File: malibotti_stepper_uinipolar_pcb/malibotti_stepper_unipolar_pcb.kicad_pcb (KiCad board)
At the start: 2 copper layers, 70 x 68 mm, 35 parts, among them J1 Stepper 1, J2 Stepper 2, J3 Servo, J4 I2C, J5 USB_C_Receptacle_USB2.0_16P, J6 Serial, SW1 RST, SW2 MicroSwitchLeft, SW3 MicroSwitchRight, SW8 BTN, U1 TBD62783A, U3 AMS1117, U5 ESP32-S3-MINI-1

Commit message: Varions
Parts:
- moved ST1 8.14 mm to (60.5, 76.0)
- moved ST2 8.14 mm to (60.5, 124.0)
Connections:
- J1 pad 1: Net-(J1-Pin_1) -> GND
- J1 pad 5: +5V -> Net-(J1-Pin_5)
- J2 pad 1: Net-(J2-Pin_1) -> GND
- J2 pad 5: +5V -> Net-(J2-Pin_5)
- U1 pad 11: Net-(J1-Pin_1) -> Net-(J1-Pin_5)
- U1 pad 12: Net-(J2-Pin_4) -> Net-(J2-Pin_2)
- U1 pad 13: Net-(J1-Pin_2) -> Net-(J1-Pin_4)
- U1 pad 16: Net-(J2-Pin_2) -> Net-(J2-Pin_4)
- U1 pad 17: Net-(J1-Pin_4) -> Net-(J1-Pin_2)
- U1 pad 18: Net-(J2-Pin_1) -> Net-(J2-Pin_5)
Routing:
- net +5V: track 139.3 -> 117.4 mm
- net Net-(J2-Pin_1): track 14.3 -> 0.00 mm
- net Net-(J2-Pin_2): track 12.3 -> 0.00 mm
- net Net-(J2-Pin_3): track 11.6 -> 0.00 mm
- net Net-(J2-Pin_4): track 10.7 -> 0.00 mm
- net Net-(J1-Pin_1): track 7.75 -> 0.00 mm
- net Net-(J1-Pin_2): track 7.25 -> 0.00 mm
- net Net-(J1-Pin_4): track 7.04 -> 0.00 mm
- net Net-(J1-Pin_3): track 6.75 -> 0.00 mm
- net Net-(J1-Pin_5): track 0.00 -> 3.06 mm
- net GND: vias 136 -> 119

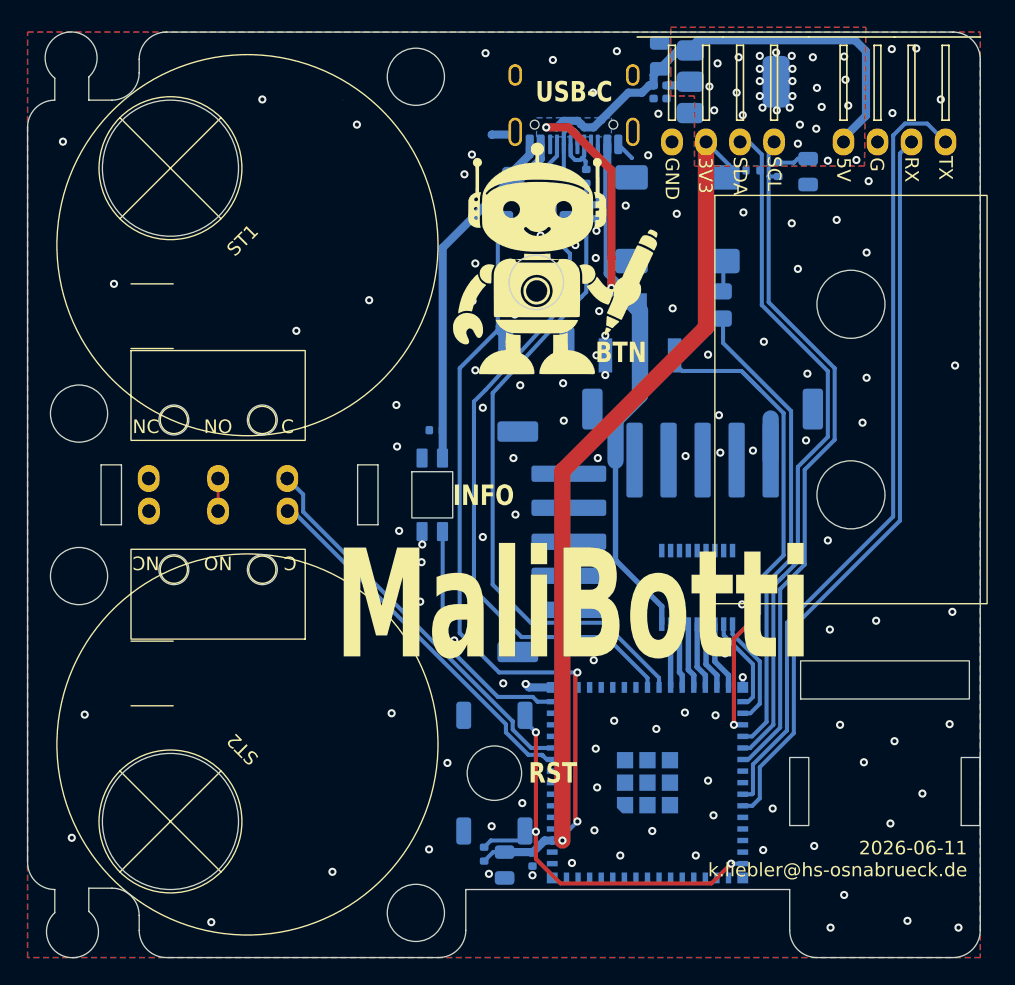
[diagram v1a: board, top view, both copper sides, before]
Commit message: Revert "Merge branch 'master' of https://github.com/klaus-liebler/malibotti"
This reverts commit e32d648555214dd673c0994955a1c8da412dea1e, reversing
changes made to 1ab6b0115ca777e0c305d243220f439b6c76d3ff.
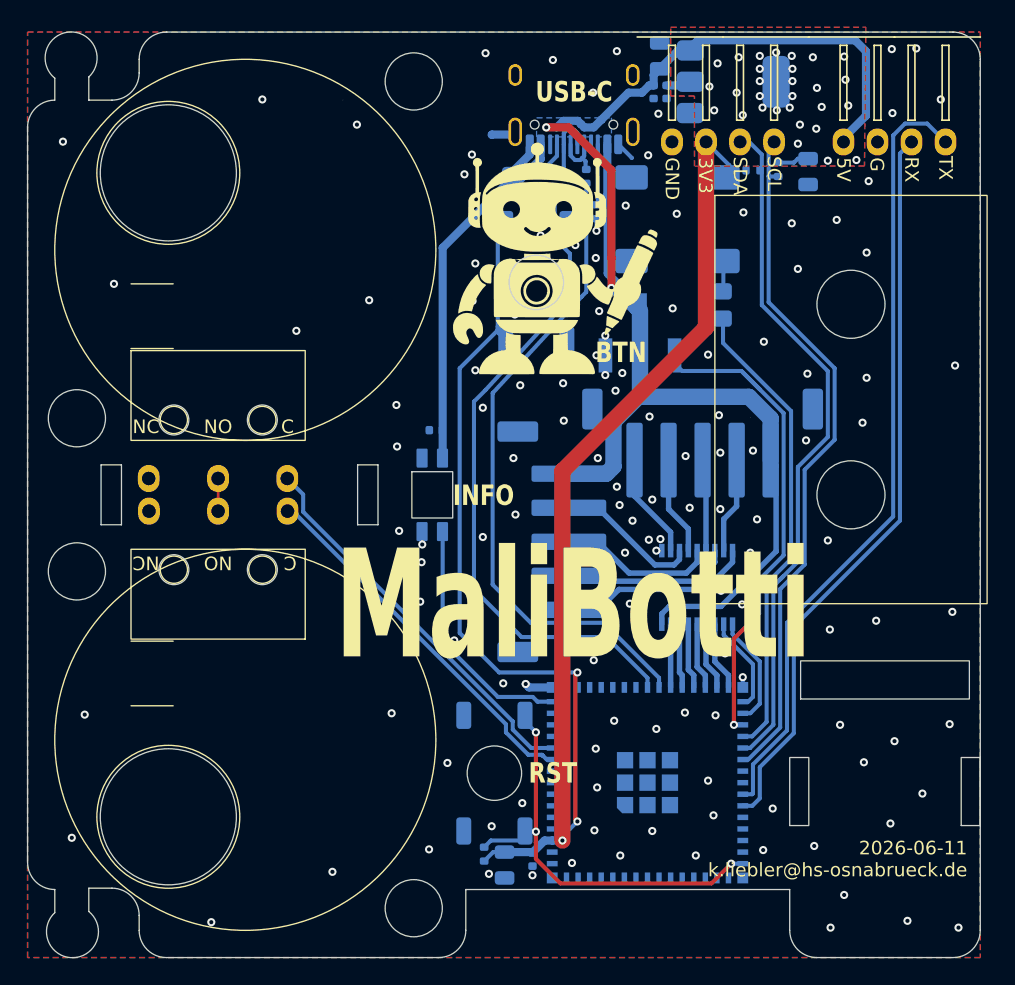
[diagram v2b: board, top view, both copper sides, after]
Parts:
- moved ST1 8.14 mm to (66.0, 82.0)
- moved ST2 8.14 mm to (66.0, 118.0)
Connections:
- J1 pad 1: GND -> Net-(J1-Pin_1)
- J1 pad 5: Net-(J1-Pin_5) -> +5V
- J2 pad 1: GND -> Net-(J2-Pin_1)
- J2 pad 5: Net-(J2-Pin_5) -> +5V
- U1 pad 11: Net-(J1-Pin_5) -> Net-(J1-Pin_1)
- U1 pad 12: Net-(J2-Pin_2) -> Net-(J2-Pin_4)
- U1 pad 13: Net-(J1-Pin_4) -> Net-(J1-Pin_2)
- U1 pad 16: Net-(J2-Pin_4) -> Net-(J2-Pin_2)
- U1 pad 17: Net-(J1-Pin_2) -> Net-(J1-Pin_4)
- U1 pad 18: Net-(J2-Pin_5) -> Net-(J2-Pin_1)
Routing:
- net +5V: track 117.4 -> 139.3 mm
- net Net-(J2-Pin_1): track 0.00 -> 14.3 mm
- net Net-(J2-Pin_2): track 0.00 -> 12.3 mm
- net Net-(J2-Pin_3): track 0.00 -> 11.6 mm
- net Net-(J2-Pin_4): track 0.00 -> 10.7 mm
- net Net-(J1-Pin_1): track 0.00 -> 7.75 mm
- net Net-(J1-Pin_2): track 0.00 -> 7.25 mm
- net Net-(J1-Pin_4): track 0.00 -> 7.04 mm
- net Net-(J1-Pin_3): track 0.00 -> 6.75 mm
- net Net-(J1-Pin_5): track 3.06 -> 0.00 mm
- net GND: vias 119 -> 136
